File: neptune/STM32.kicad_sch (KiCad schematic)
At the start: 19 parts, among them SW1 TS-1187A-B-A-B, SW2 TS-1187A-B-A-B, U6 STM32F411RETx, Y1 12MHz, Y2 32.768k

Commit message: Updated some footprints, restarted routing
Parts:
- C15, C16, C17, C18: footprint Capacitor_SMD:C_0805_2012Metric -> Capacitor_SMD:C_0603_1608Metric
- SW1, SW2: footprint Button_Switch_SMD:SW_Push_1P1T_NO_CK_KSC6xxJ -> Button_Switch_SMD:SW_Tactile_SPST_NO_Straight_CK_PTS636Sx25SMTRLFS
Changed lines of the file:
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@@
       (effects (font (size 1.27 1.27)) (justify left))
     )
-    (property "Footprint" "Capacitor_SMD:C_0805_2012Metric" (at 113.03 69.85 0)
+    (property "Footprint" "Capacitor_SMD:C_0603_1608Metric" (at 113.03 69.85 0)
       (effects (font (size 1.27 1.27)) hide)
     )
@@
       (effects (font (size 1.27 1.27)))
     )
-    (property "Footprint" "Button_Switch_SMD:SW_Push_1P1T_NO_CK_KSC6xxJ" (at 33.02 40.64 0)
+    (property "Footprint" "Button_Switch_SMD:SW_Tactile_SPST_NO_Straight_CK_PTS636Sx25SMTRLFS" (at 33.02 40.64 0)
       (effects (font (size 1.27 1.27)) hide)
     )
@@
       (effects (font (size 1.27 1.27)) (justify left))
     )
-    (property "Footprint" "Capacitor_SMD:C_0805_2012Metric" (at 113.03 43.18 0)
+    (property "Footprint" "Capacitor_SMD:C_0603_1608Metric" (at 113.03 43.18 0)
       (effects (font (size 1.27 1.27)) hide)
     )
@@
       (effects (font (size 1.27 1.27)) (justify left))
     )
-    (property "Footprint" "Capacitor_SMD:C_0805_2012Metric" (at 125.73 69.85 0)
+    (property "Footprint" "Capacitor_SMD:C_0603_1608Metric" (at 125.73 69.85 0)
       (effects (font (size 1.27 1.27)) hide)
     )
@@
       (effects (font (size 1.27 1.27)) (justify left))
     )
-    (property "Footprint" "Capacitor_SMD:C_0805_2012Metric" (at 125.73 43.18 0)
+    (property "Footprint" "Capacitor_SMD:C_0603_1608Metric" (at 125.73 43.18 0)
       (effects (font (size 1.27 1.27)) hide)
     )
@@
       (effects (font (size 1.27 1.27)))
     )
-    (property "Footprint" "Button_Switch_SMD:SW_Push_1P1T_NO_CK_KSC6xxJ" (at 62.23 48.26 0)
-      (effects (font (size 1.27 1.27)) hide)
-    )
+    (property "Footprint" "Button_Switch_SMD:SW_Tactile_SPST_NO_Straight_CK_PTS636Sx25SMTRLFS" (at 62.23 48.26 0)
+      (effects (font (size 1.27 1.27)) hide)
+    )

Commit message: Continued routing
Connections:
- net WP_FC: now reaches U6.59 (PB7)
- net HOLD_FC: now reaches U6.61 (PB8)
- net CS_FC: now reaches U6.62 (PB9)
- net CLK_SD renamed SCK_FC
- net CS_SD: no longer names the net of U6.11 (PC3)
- net MISO_SD renamed MISO_FC
- net MOSI_SD renamed MOSI_FC
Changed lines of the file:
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@@
+    (stroke (width 0) (type default))
+  )
+  (wire (pts (xy 252.73 106.68) (xy 248.92 106.68))
     (stroke (width 0) (type default))
   )
@@
     (stroke (width 0) (type default))
   )
+  (wire (pts (xy 248.92 101.6) (xy 252.73 101.6))
+    (stroke (width 0) (type default))
+  )
   (wire (pts (xy 226.06 125.73) (xy 228.6 125.73))
     (stroke (width 0) (type default))
@@
     (stroke (width 0) (type default))
   )
-  (wire (pts (xy 209.55 88.9) (xy 213.36 88.9))
-    (stroke (width 0) (type default))
-  )
   (wire (pts (xy 163.83 35.56) (xy 157.48 35.56))
+    (stroke (width 0) (type default))
+  )
+  (wire (pts (xy 248.92 104.14) (xy 252.73 104.14))
     (stroke (width 0) (type default))
   )
@@
     (effects (font (size 1.27 1.27)) (justify left bottom))
   )
-  (hierarchical_label "CS_SD" (shape output) (at 209.55 88.9 180) (fields_autoplaced)
-    (effects (font (size 1.27 1.27)) (justify right))
-  )
-  (hierarchical_label "CLK_SD" (shape output) (at 209.55 106.68 180) (fields_autoplaced)
+  (hierarchical_label "CS_FC" (shape output) (at 252.73 106.68 0) (fields_autoplaced)
+    (effects (font (size 1.27 1.27)) (justify left))
+  )
+  (hierarchical_label "SCK_FC" (shape output) (at 209.55 106.68 180) (fields_autoplaced)
     (effects (font (size 1.27 1.27)) (justify right))
   )
@@
     (effects (font (size 1.27 1.27)) (justify right))
   )
+  (hierarchical_label "WP_FC" (shape output) (at 252.73 101.6 0) (fields_autoplaced)
+    (effects (font (size 1.27 1.27)) (justify left))
+  )
   (hierarchical_label "IMU_SCK" (shape output) (at 252.73 53.34 0) (fields_autoplaced)
     (effects (font (size 1.27 1.27)) (justify left))
   )
-  (hierarchical_label "MOSI_SD" (shape output) (at 209.55 111.76 180) (fields_autoplaced)
+  (hierarchical_label "MOSI_FC" (shape output) (at 209.55 111.76 180) (fields_autoplaced)
     (effects (font (size 1.27 1.27)) (justify right))
   )
@@
     (effects (font (size 1.27 1.27)) (justify left))
   )
-  (hierarchical_label "MISO_SD" (shape input) (at 209.55 109.22 180) (fields_autoplaced)
+  (hierarchical_label "MISO_FC" (shape input) (at 209.55 109.22 180) (fields_autoplaced)
     (effects (font (size 1.27 1.27)) (justify right))
   )
@@
     (effects (font (size 1.27 1.27)) (justify left))
   )
+  (hierarchical_label "HOLD_FC" (shape output) (at 252.73 104.14 0) (fields_autoplaced)
+    (effects (font (size 1.27 1.27)) (justify left))
+  )

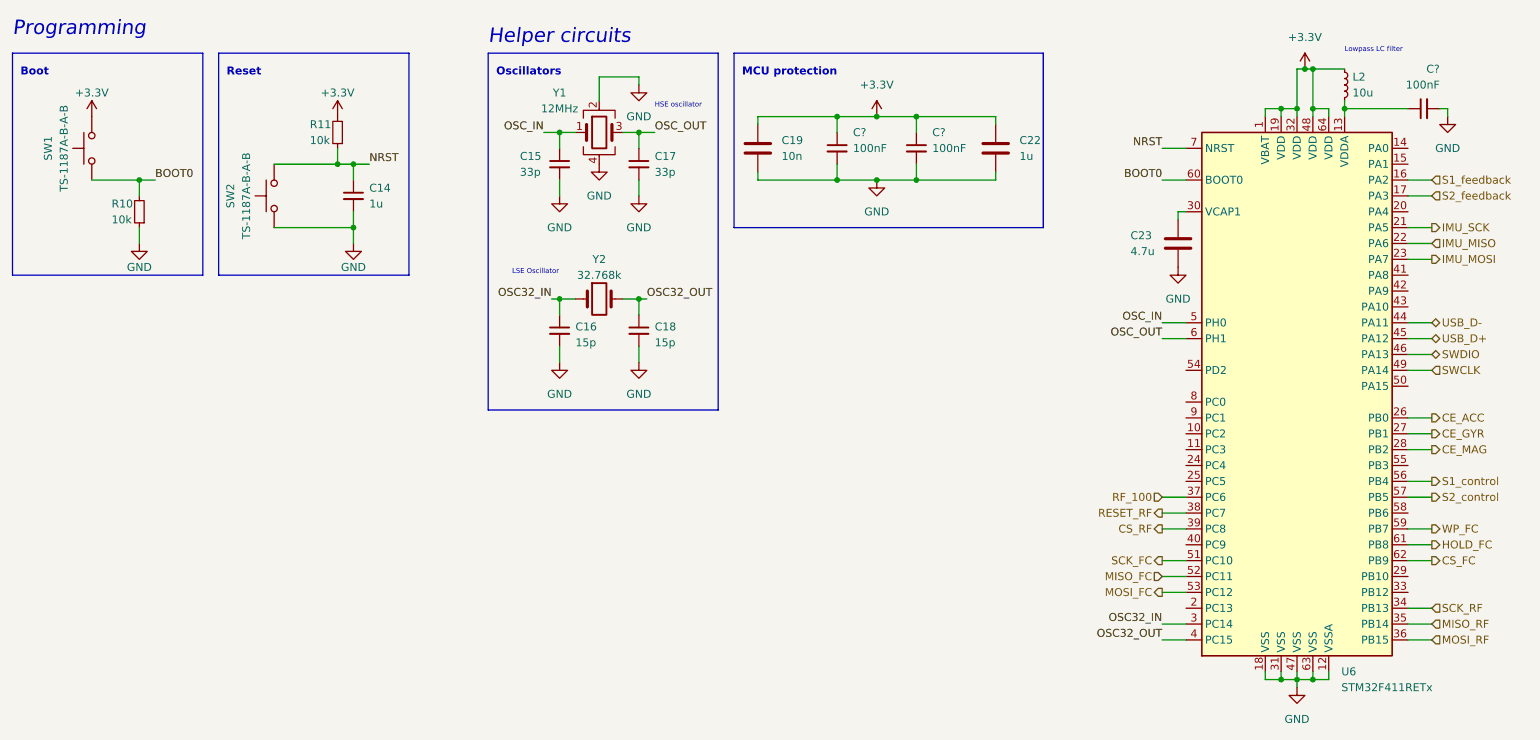
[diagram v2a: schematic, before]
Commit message: Routed 3.3V stepdown, added indicator LEDs
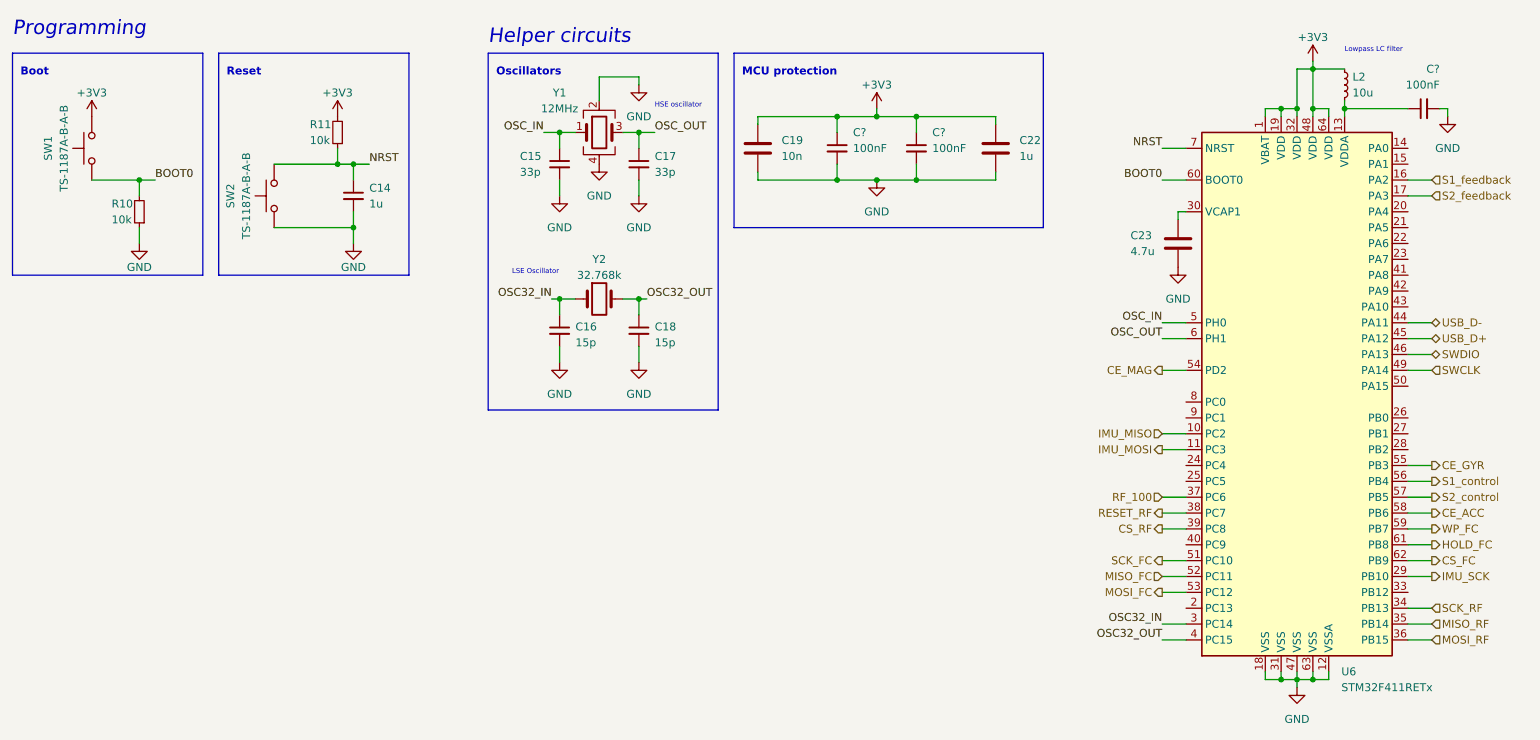
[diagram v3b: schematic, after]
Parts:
- L2: footprint Inductor_SMD:L_0805_2012Metric -> Inductor_SMD:L_0603_1608Metric
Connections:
- net CE_ACC: now also U6.58 (PB6); no longer U6.26 (PB0)
- net CE_GYR: now also U6.55 (PB3); no longer U6.27 (PB1)
- net CE_MAG: now also U6.54 (PD2); no longer U6.28 (PB2)
- net IMU_MISO: now also U6.10 (PC2); no longer U6.22 (PA6)
- net IMU_MOSI: now also U6.11 (PC3); no longer U6.23 (PA7)
- net IMU_SCK: now also U6.29 (PB10); no longer U6.21 (PA5)
